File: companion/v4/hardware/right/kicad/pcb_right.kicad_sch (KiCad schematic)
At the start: 19 parts, among them J1 TF31-6S-0.5SH_800_, J2 speaker, SW1 SW_Push, U1 AP2112K-3.3, U2 MAX98357AETE_T, U3 ESP32-C6-MINI-1

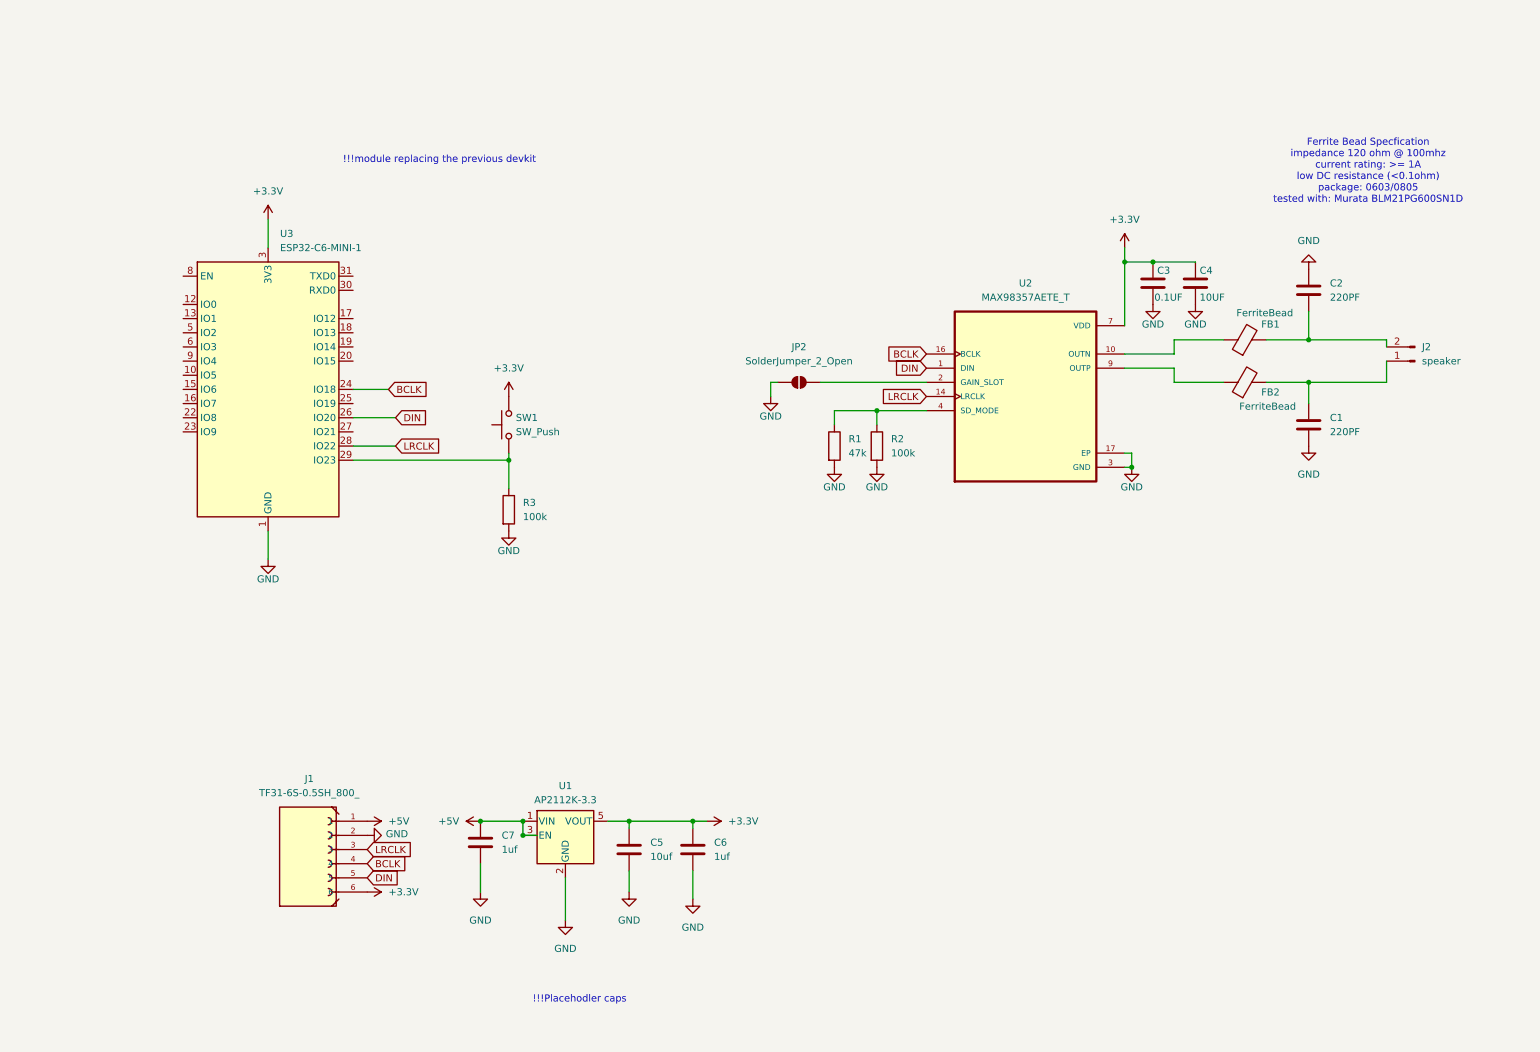
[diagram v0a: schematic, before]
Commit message: box organiziers
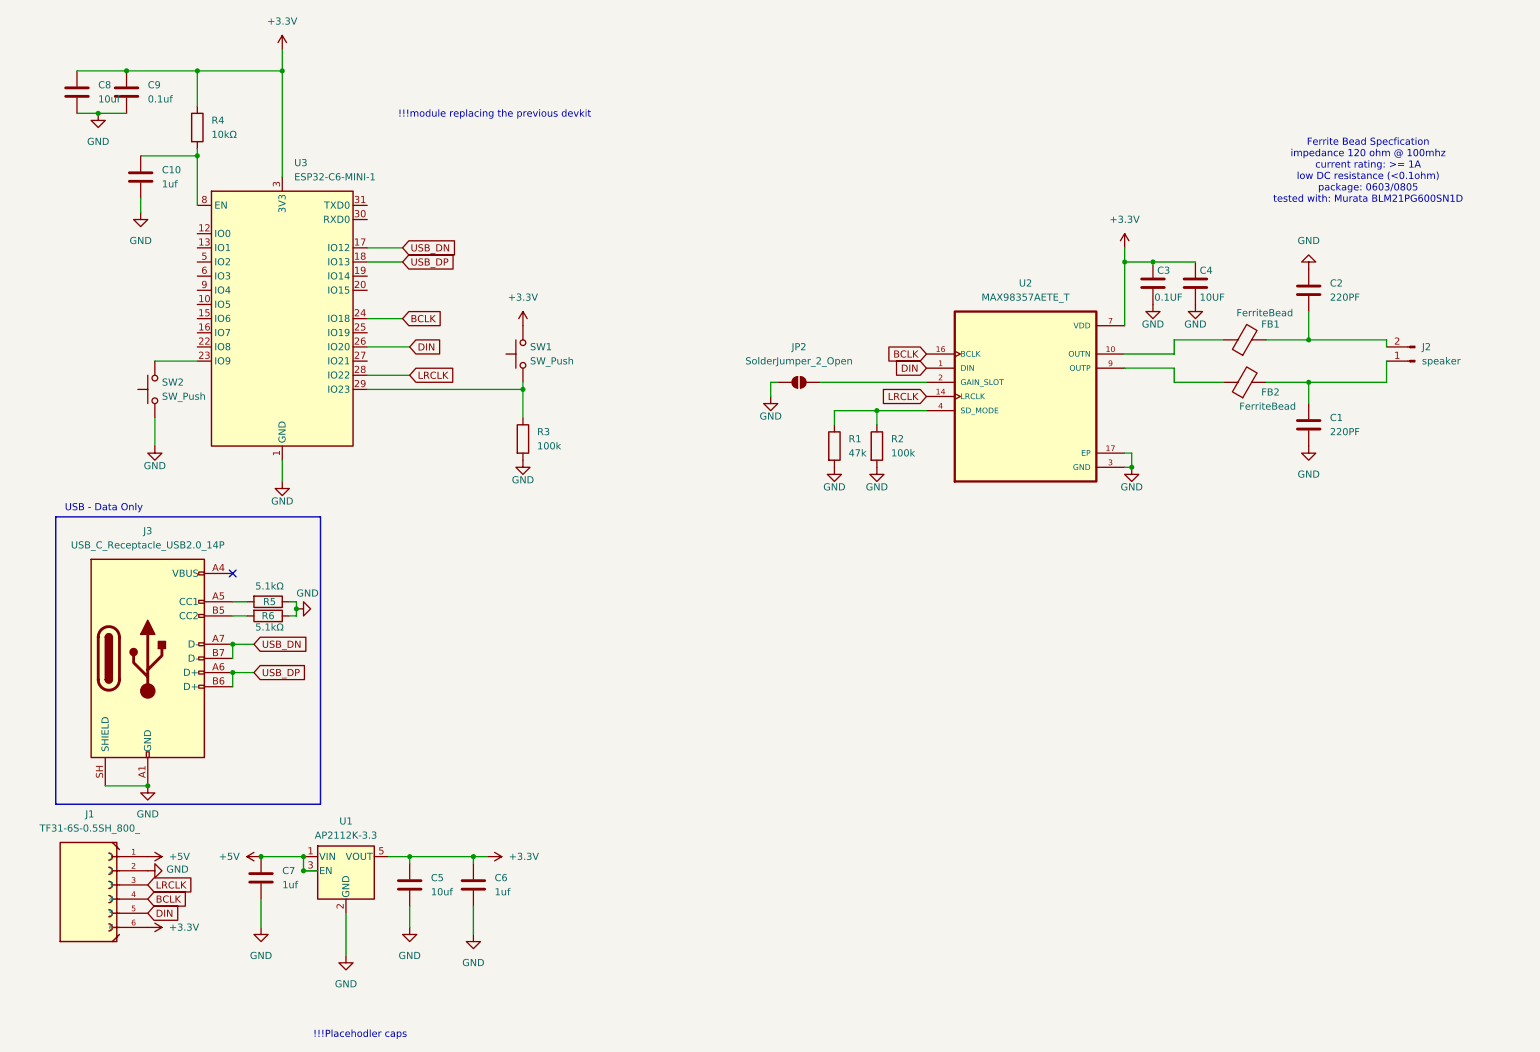
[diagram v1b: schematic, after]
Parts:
- added C10: 1uf, symbol Device:C
- added C8: 10uf, symbol Device:C
- added C9: 0.1uf, symbol Device:C
- added J3: USB_C_Receptacle_USB2.0_14P, symbol Connector:USB_C_Receptacle_USB2.0_14P
- added R4: 10kΩ, symbol Device:R
- added R5, R6: 5.1kΩ, symbol Device:R
- added SW2: SW_Push, symbol Switch:SW_Push
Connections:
- net +3.3V: now also C8.1, C9.1, R4.1
- net GND: now also C10.2, C8.2, C9.2, J3.A1 (GND), J3.A12 (GND), J3.B1 (GND), J3.B12 (GND), J3.SH (SHIELD), R5.1, R6.1, SW2.1
- net USB_DN: now reaches U3.17 (IO12)
- net USB_DN: now also J3.A7 (D-), J3.B7 (D-)
- net USB_DP: now reaches U3.18 (IO13)
- net USB_DP: now also J3.A6 (D+), J3.B6 (D+)
- net at U3.23 (IO9): now also SW2.2
- net at U3.8 (EN): now also C10.1, R4.2
- new net: J3.A5 (CC1), R5.2
- new net: J3.B5 (CC2), R6.2
- new net: J3.A4 (VBUS), J3.A9 (VBUS), J3.B4 (VBUS), J3.B9 (VBUS)
- no-connect marks 0 -> 1
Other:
- note added: "USB - Data Only"
- moved on the sheet: C5, C6, C7, J1, R3, SW1, U1, U3

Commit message: fixes
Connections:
- net +3.3V: now also C1.2, C10.2, C2.1, C3.2, C4.2, C5.2, C6.2, C7.2, J1.2, J3.A1 (GND), J3.A12 (GND), J3.B1 (GND), J3.B12 (GND), J3.SH (SHIELD), JP2.1 (A), R1.2, R2.2, R3.2, R5.1, R6.1, SW2.1, U1.2 (GND), U2.11 (GND), U2.15 (GND), U2.17 (EP), U2.3 (GND), U3.1 (GND), U3.11 (GND), U3.14 (GND), U3.2 (GND), U3.36 (GND), U3.37 (GND), U3.38 (GND), U3.39 (GND), U3.40 (GND), U3.41 (GND), U3.42 (GND), U3.43 (GND), U3.44 (GND), U3.45 (GND), U3.46 (GND), U3.47 (GND), U3.48 (GND), U3.49 (GND), U3.50 (GND), U3.51 (GND), U3.52 (GND), U3.53 (GND)
- removed net GND: C1.2, C10.2, C2.1, C3.2, C4.2, C5.2, C6.2, C7.2, C8.2, C9.2, J1.2, J3.A1 (GND), J3.A12 (GND), J3.B1 (GND), J3.B12 (GND), J3.SH (SHIELD), JP2.1 (A), R1.2, R2.2, R3.2, R5.1, R6.1, SW2.1, U1.2 (GND), U2.11 (GND), U2.15 (GND), U2.17 (EP), U2.3 (GND), U3.1 (GND), U3.11 (GND), U3.14 (GND), U3.2 (GND), U3.36 (GND), U3.37 (GND), U3.38 (GND), U3.39 (GND), U3.40 (GND), U3.41 (GND), U3.42 (GND), U3.43 (GND), U3.44 (GND), U3.45 (GND), U3.46 (GND), U3.47 (GND), U3.48 (GND), U3.49 (GND), U3.50 (GND), U3.51 (GND), U3.52 (GND), U3.53 (GND)
- new net: C8.2, C9.2
- no-connect marks 1 -> 16
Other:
- note added: "3.3V Regulator"
- note added: "ESP-32-C6 Microcontroller"
- note added: "Left Board Connector"
- note removed: "!!!Placehodler caps"
- note removed: "!!!module replacing the previous devkit"
- moved on the sheet: C10, C5, C6, C7, C8, C9, J1, R3, R4, SW1, SW2, U1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

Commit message: Camera connector
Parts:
- added C11, C12, C14, C15: 1uf, symbol Device:C
- added C13: 100n, symbol Device:C
- added J4: Conn_01x24_MountingPin, Connector_FFC-FPC:Hirose_FH12-24S-0.5SH_1x24-1MP_P0.50mm_Horizontal, symbol Connector_Generic_MountingPin:Conn_01x24_MountingPin
- added R10, R9: 10k, Resistor_SMD:R_0805_2012Metric_Pad1.20x1.40mm_HandSolder, symbol Device:R
- added R7, R8: 4.7k, Resistor_SMD:R_0805_2012Metric_Pad1.20x1.40mm_HandSolder, symbol Device:R
- added U4: ESP32-S3-MINI-1, RF_Module:ESP32-S2-MINI-1, symbol RF_Module:ESP32-S3-MINI-1
- added U5: TLV75528PDBV, Package_TO_SOT_SMD:SOT-23-5, symbol Regulator_Linear:TLV75528PDBV
- added U7: TLV75515PDBV, Package_TO_SOT_SMD:SOT-23-5, symbol Regulator_Linear:TLV75515PDBV
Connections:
- net +3.3V: now also C11.1, C14.1, J4.11 (Pin_11), R7.1, R8.1, R9.1, U5.1 (IN), U5.3 (EN), U7.1 (IN), U7.3 (EN); no longer C1.2, C10.2, C2.1, C3.2, C4.2, C5.2, C6.2, C7.2, J1.2, J3.A1 (GND), J3.A12 (GND), J3.B1 (GND), J3.B12 (GND), J3.SH (SHIELD), JP2.1 (A), R1.2, R2.2, R3.2, R5.1, R6.1, SW2.1, U1.2 (GND), U2.11 (GND), U2.15 (GND), U2.17 (EP), U2.3 (GND), U3.1 (GND), U3.11 (GND), U3.14 (GND), U3.2 (GND), U3.36 (GND), U3.37 (GND), U3.38 (GND), U3.39 (GND), U3.40 (GND), U3.41 (GND), U3.42 (GND), U3.43 (GND), U3.44 (GND), U3.45 (GND), U3.46 (GND), U3.47 (GND), U3.48 (GND), U3.49 (GND), U3.50 (GND), U3.51 (GND), U3.52 (GND), U3.53 (GND)
- net GND: now reaches C8.2, C9.2
- net GND: now also C1.2, C10.2, C2.1, C3.2, C4.2, C5.2, C6.2, C7.2, J1.2, J3.A1 (GND), J3.A12 (GND), J3.B1 (GND), J3.B12 (GND), J3.SH (SHIELD), JP2.1 (A), R1.2, R2.2, R3.2, R5.1, R6.1, SW2.1, U1.2 (GND), U2.11 (GND), U2.15 (GND), U2.17 (EP), U2.3 (GND), U3.1 (GND), U3.11 (GND), U3.14 (GND), U3.2 (GND), U3.36 (GND), U3.37 (GND), U3.38 (GND), U3.39 (GND), U3.40 (GND), U3.41 (GND), U3.42 (GND), U3.43 (GND), U3.44 (GND), U3.45 (GND), U3.46 (GND), U3.47 (GND), U3.48 (GND), U3.49 (GND), U3.50 (GND), U3.51 (GND), U3.52 (GND), U3.53 (GND), C11.2, C12.2, C13.1, C14.2, C15.2, J4.15 (Pin_15), J4.2 (Pin_2), J4.MP (MountPin), R10.1, U4.1 (GND), U4.2 (GND), U4.42 (GND), U4.43 (GND), U4.46 (GND), U4.47 (GND), U4.48 (GND), U4.49 (GND), U4.50 (GND), U4.51 (GND), U4.52 (GND), U4.53 (GND), U4.54 (GND), U4.55 (GND), U4.56 (GND), U4.57 (GND), U4.58 (GND), U4.59 (GND), U4.60 (GND), U4.61 (GND), U4.62 (GND), U4.63 (GND), U4.64 (GND), U4.65 (GND), U5.2 (GND), U7.2 (GND)
- new net +2.8V: C12.1, J4.4 (Pin_4), U5.5 (OUT)
- new net CAM_HREF: J4.9 (Pin_9), U4.27 (IO47)
- new net CAM_PLCK: J4.17 (Pin_17), U4.17 (IO13)
- new net CAM_PWDN: J4.8 (Pin_8), R10.2
- new net CAM_RESET: C13.2, J4.6 (Pin_6), R9.2
- new net CAM_SIOC: J4.5 (Pin_5), R8.2, U4.35 (IO39)
- new net CAM_SIOD: J4.3 (Pin_3), R7.2, U4.36 (IO40)
- new net CAM_VSYNC: J4.7 (Pin_7), U4.34 (IO38)
- new net CAM_XCLK: J4.13 (Pin_13), U4.14 (IO10)
- new net CAM_Y2: J4.19 (Pin_19), U4.19 (IO15)
- new net CAM_Y3: J4.21 (Pin_21), U4.21 (IO17)
- new net CAM_Y4: J4.22 (Pin_22), U4.22 (IO18)
- new net CAM_Y5: J4.20 (Pin_20), U4.20 (IO16)
- new net CAM_Y6: J4.18 (Pin_18), U4.18 (IO14)
- new net CAM_Y7: J4.16 (Pin_16), U4.16 (IO12)
- new net CAM_Y8: J4.14 (Pin_14), U4.15 (IO11)
- new net CAM_Y9: J4.12 (Pin_12), U4.30 (IO48)
- new net DVDD: C15.1, J4.10 (Pin_10), U7.5 (OUT)
- no-connect marks 16 -> 19
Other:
- note added: "1.5 V Voltage Regulator (DVDD) / 1.2V for 0V2640"
- note added: "2.8V Voltage Regulator"
- note added: "ESP-32-C6 Microcontroller - DNP!!!, replace with ESP-S3"
- note removed: "ESP-32-C6 Microcontroller"
- moved on the sheet: C1, C2, C3, C4, C5, C6, C7, FB1, FB2, J1, J2, JP2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

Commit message: ESP-32-S3
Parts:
- removed R3: 100k, Resistor_SMD:R_0805_2012Metric_Pad1.20x1.40mm_HandSolder, symbol Device:R
- removed SW2: SW_Push, symbol Switch:SW_Push
- removed U3: ESP32-C6-MINI-1, RF_Module:ESP32-C6-MINI-1, symbol RF_Module:ESP32-C6-MINI-1
- added C16: 100n, symbol Device:C
- added R11: 10kΩ, symbol Device:R
- added SW3: SW_RESET, Button_Switch_THT:SW_PUSH_6mm_H5mm, symbol Switch:SW_Push
- added TP1: TestPoint, Package_TO_SOT_SMD:SOT-23-5, symbol Connector:TestPoint
- added TP2: TestPoint, symbol Connector:TestPoint
- added U3: USBLC6-2SC6, Package_TO_SOT_SMD:SOT-23-6, symbol Power_Protection:USBLC6-2SC6
- C10: value 1uf -> 1u
- C8: value 10uf -> 10u
- C9: value 0.1uf -> 0.1u
- SW1: value SW_Push -> SW_BOOT
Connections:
- net +3.3V: now also U4.3 (3V3), C16.2, R11.2, U3.5 (VBUS); no longer SW1.2
- net BCLK: now also U4.9 (IO5)
- net CAM_PWDN: now also U4.25 (IO21)
- net DIN: now also U4.8 (IO4)
- net GND: now also SW1.1, C16.1, SW3.2, U3.2 (GND)
- net LRCLK: now also U4.10 (IO6)
- net USB_DN: now also U4.23 (USB_D-), U3.3 (I/O2), U3.4 (I/O2)
- net USB_DP: now also U4.24 (USB_D+), U3.1 (I/O1), U3.6 (I/O1)
- net at C10.1, R4.2: now also U4.45 (EN), SW3.1
- net at U4.39 (TXD0): now also TP1.1
- net at U4.4 (IO0): now also SW1.2, R11.1
- net at U4.40 (RXD0): now also TP2.1
- net CAM_PLCK renamed CAM_PCLK
- no-connect marks 19 -> 20
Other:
- note added: "ESD Protection"
- note removed: "ESP-32-C6 Microcontroller - DNP!!!, replace with ESP-S3"
- moved on the sheet: C1, C11, C12, C13, C2, C3, C4, C5, C6, C7, FB1, FB2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
